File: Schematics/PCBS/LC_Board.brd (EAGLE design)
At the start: 160 x 100 mm, 24 parts, among them IC1 ATMEGA328P-AU, Q10 220mA/50V/3.5Ω, U1 LT1763CS8-3.3#TRPBF

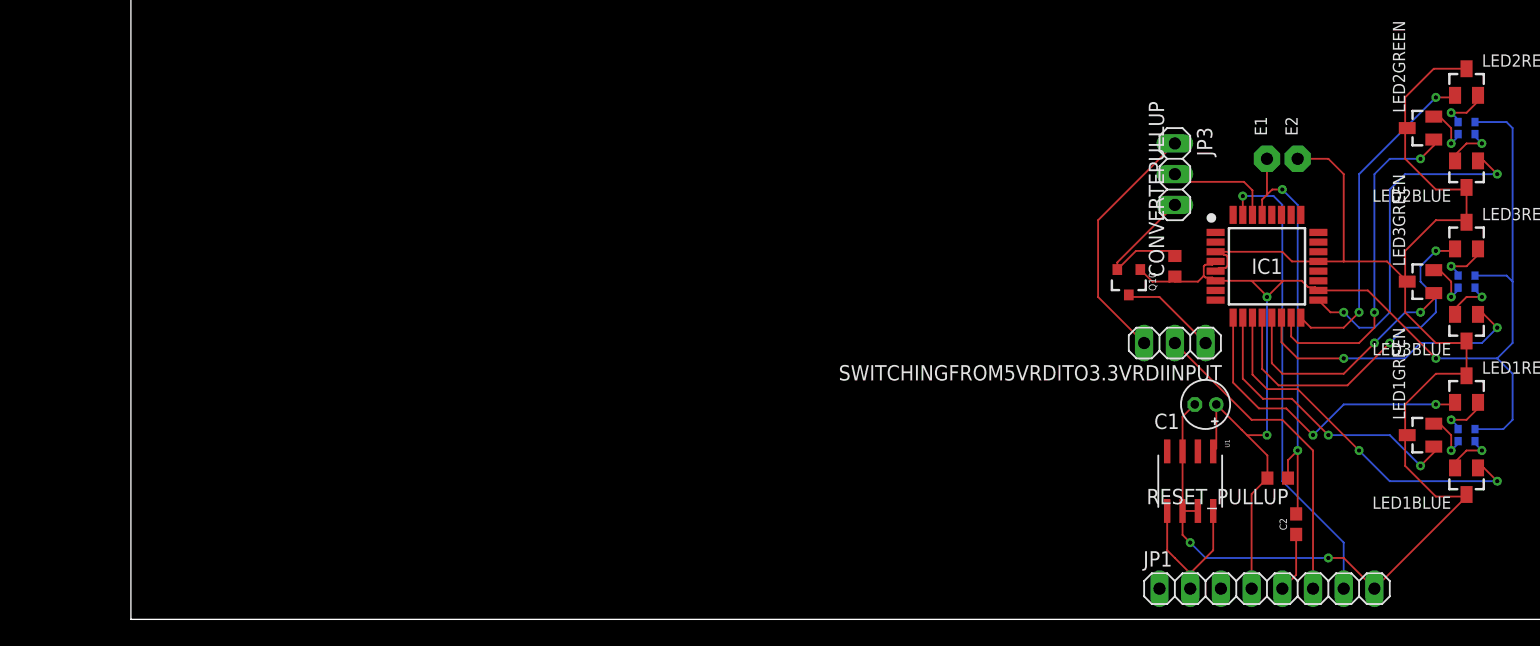
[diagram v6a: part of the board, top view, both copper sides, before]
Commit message: updated LC_Board IO to match need pins for Shift registers
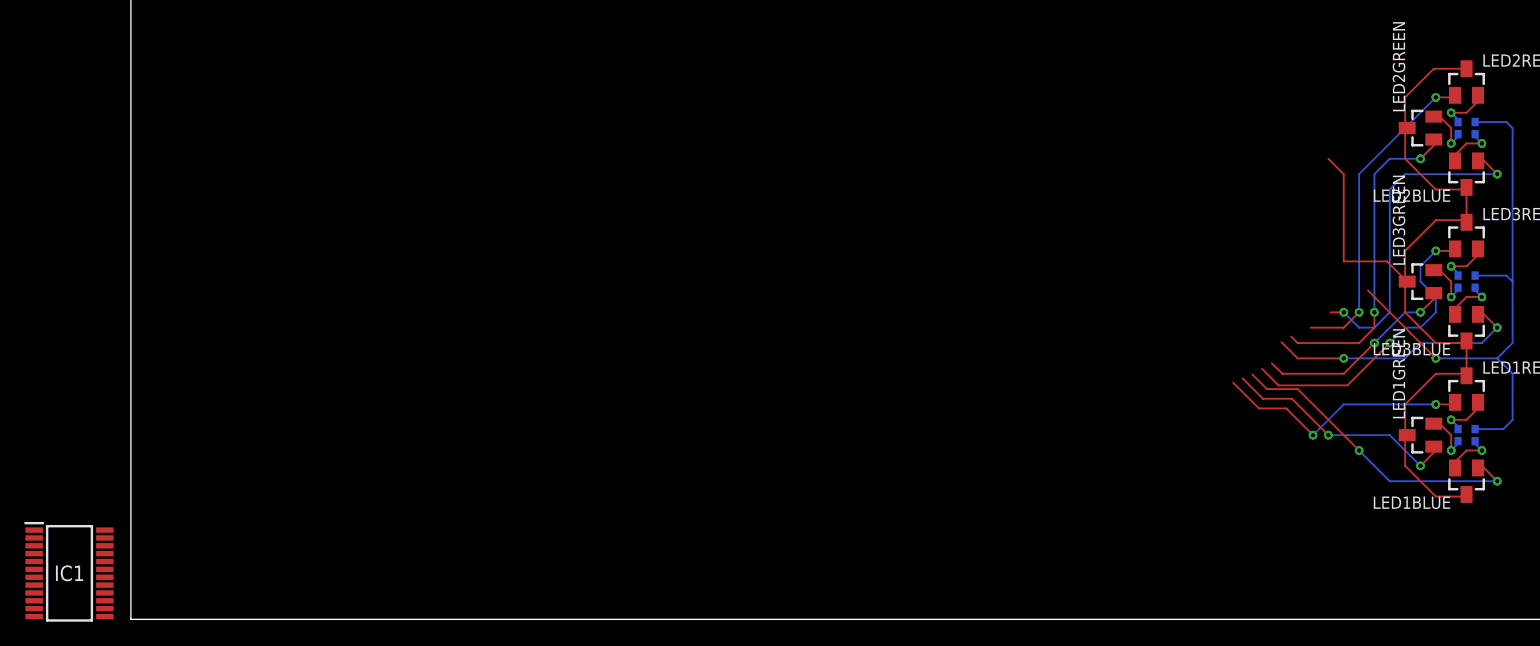
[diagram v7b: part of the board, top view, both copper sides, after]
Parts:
- removed C1: 10uf, adafruit:E1,8-4
- removed C2: 0.1uF, SparkFun-Capacitors:0603
- removed CONVERTEPULLUP, RESET_PULLUP: 10K, audio amplifier example:R0603
- removed E1, E2: DPADS_PAD-0400-S, 52101-101-REV-A:DPADS_0400-S
- removed JP1: IO, pinhead:1X08
- removed JP3: (no value), pinhead:1X03
- removed Q10: 220mA/50V/3.5Ω, SparkFun-DiscreteSemi:SOT23-3
- removed SWITCHINGFROM5VRDITO3.3VRDIINPUT: Switch4RXI INPUT, pinhead:1X03
- removed U1: LT1763CS8-3.3#TRPBF, LT1763CS8-3.3_TRPBF:SO-8_S
- IC1: value ATMEGA328P-AU -> STP16C596M; device ATMEGA328P-AU:QFP80P900X900X120-32N -> STP16C596M:SOP65P638X110-24N
- moved IC1 102.3 mm to (-5.08, 3.81)
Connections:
- removed net 2BD: JP1.1
- removed net 5V_RAIL: JP1.3
- removed net PULLED_UP3.3VRX: CONVERTEPULLUP.2, JP3.3, Q10.2
- removed net RESET_IN: C2.1, JP1.5
- removed net RESET_LINE: C2.2, E1.PAD, IC1.29, RESET_PULLUP.1
- removed net RXD_IN: Q10.3, SWITCHINGFROM5VRDITO3.3VRDIINPUT.1
- removed net RXI: JP1.6, SWITCHINGFROM5VRDITO3.3VRDIINPUT.2
- removed net RXI2: IC1.30, JP3.2
- removed net RXI_3.3V: JP3.1, SWITCHINGFROM5VRDITO3.3VRDIINPUT.3
- removed net TXO: IC1.31, JP1.7
- removed net VIN: JP1.2, U1.5, U1.8
- net 3.3V_RAIL: no longer C1.+, CONVERTEPULLUP.1, IC1.18, IC1.4, IC1.6, JP1.4, Q10.1, RESET_PULLUP.2, U1.1
- net D10: no longer IC1.14
- net D11: no longer IC1.15
- net D12: no longer IC1.16
- net D13: no longer IC1.17
- net D5: no longer IC1.9
- net D6: no longer IC1.10
- net D7: no longer IC1.11
- net D8: no longer IC1.12
- net D9: no longer IC1.13
- net GND: now also IC1.1; no longer C1.-, E2.PAD, IC1.21, IC1.3, IC1.5, JP1.8, U1.3, U1.6, U1.7
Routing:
- net 3.3V_RAIL: track 109.5 -> 48.3 mm, vias 3 -> 1
- net GND: track 131.4 -> 73.7 mm, vias 2 -> 0
- net TXO: track 39.0 -> 0.00 mm, vias 1 -> 0
- net RESET_LINE: track 36.3 -> 0.00 mm, vias 2 -> 0
- net RXI: track 26.5 -> 0.00 mm
- net RXI_3.3V: track 20.7 -> 0.00 mm
- net VIN: track 13.2 -> 0.00 mm
- net PULLED_UP3.3VRX: track 12.9 -> 0.00 mm
- net RXI2: track 9.01 -> 0.00 mm
- net RXD_IN: track 8.00 -> 0.00 mm
- net D5: track 26.7 -> 21.3 mm
- net D6: track 24.9 -> 19.9 mm
- net RESET_IN: track 4.96 -> 0.00 mm
- net D7: track 30.7 -> 25.9 mm
- net D8: track 29.5 -> 25.2 mm
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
